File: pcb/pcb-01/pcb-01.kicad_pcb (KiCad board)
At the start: 4 copper layers, 78 x 58 mm, 167 parts, among them J1 POWER, J2 MOTOR, J3 HALL, J4 TEMP, J5 I2C, J6 USB-C, J7 PROGRAM, J8 DNP 2x5 1.27mm, Q1 DMP6023LE-13, Q2 2N7002K, Q3 2N7002, SW1 SW_Push, SW2 SW_Push, SW3 SW_Push, U1 MCF8316DVRGFR, U10 SN74LVC1G17DCKR, U11 SN74LVC1G17DCKR, U12 TPD2EUSB30, U2 ESP32-C6-MINI-1, U3 TPSM365R6V3RDNR, U4 TPS7A1601DGN, U5 SN74LVC1G74DCTR, U6 SN74LVC1G74DCTR, U7 TPS3435CAKAGDD, U8 LM2907M-14, U9 TLV1701DBV

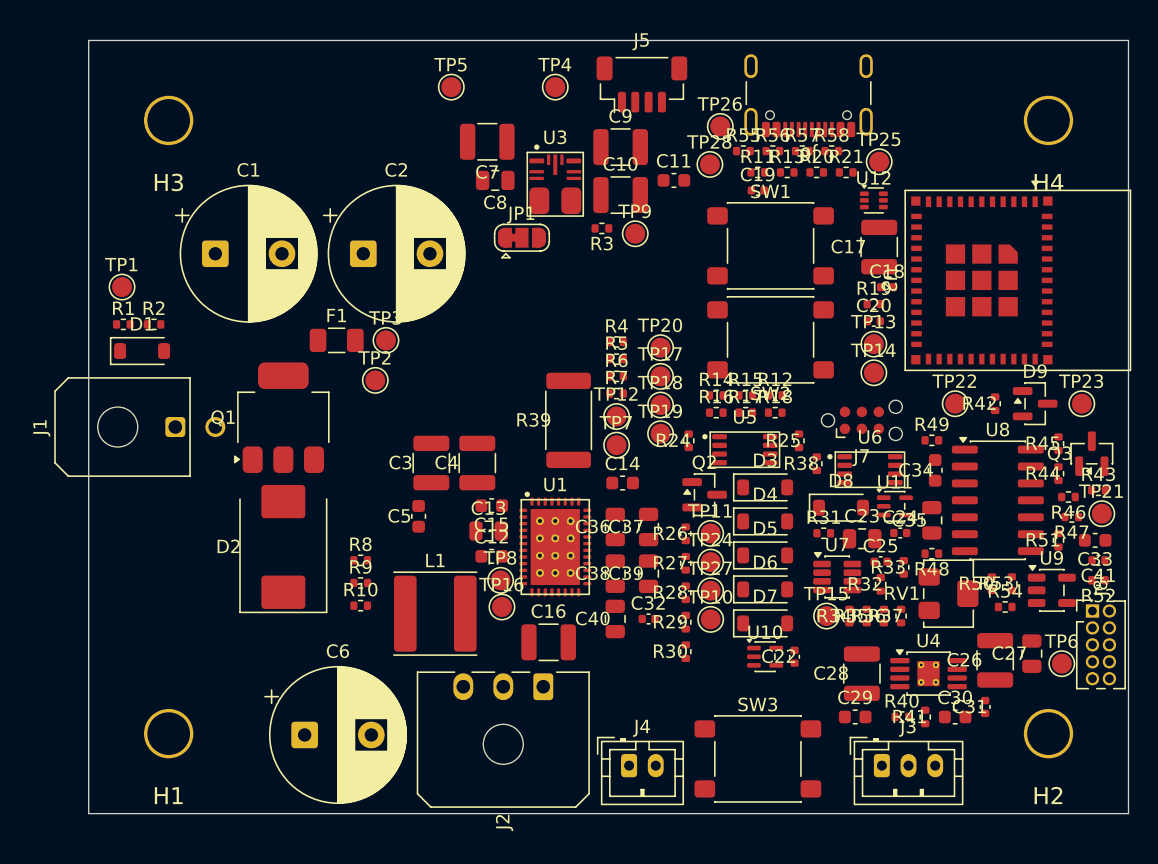
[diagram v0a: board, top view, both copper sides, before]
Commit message: pcb: aesthetic alignment pass on placement
Column/row alignment and grid snapping across all placement groups (62 parts
nudged): ESP resistor banks column-aligned, permission-cluster R/TP/D columns
on uniform pitch with aligned rows, mcf_east ladder+TP columns, lock_wd row
snapped, tach edge columns, LDO bottom row, DNP bank pitch equalized, R39
centered on U1's axis. Verified move-by-move against the exact courtyard
model (aes_check.py pattern: no gap regressions below 0.15mm except bodiless
test-point rings, documented). DRC: courtyards_overlap 16->17 (one TP ring
pair from uniform pitch), all other classes unchanged.
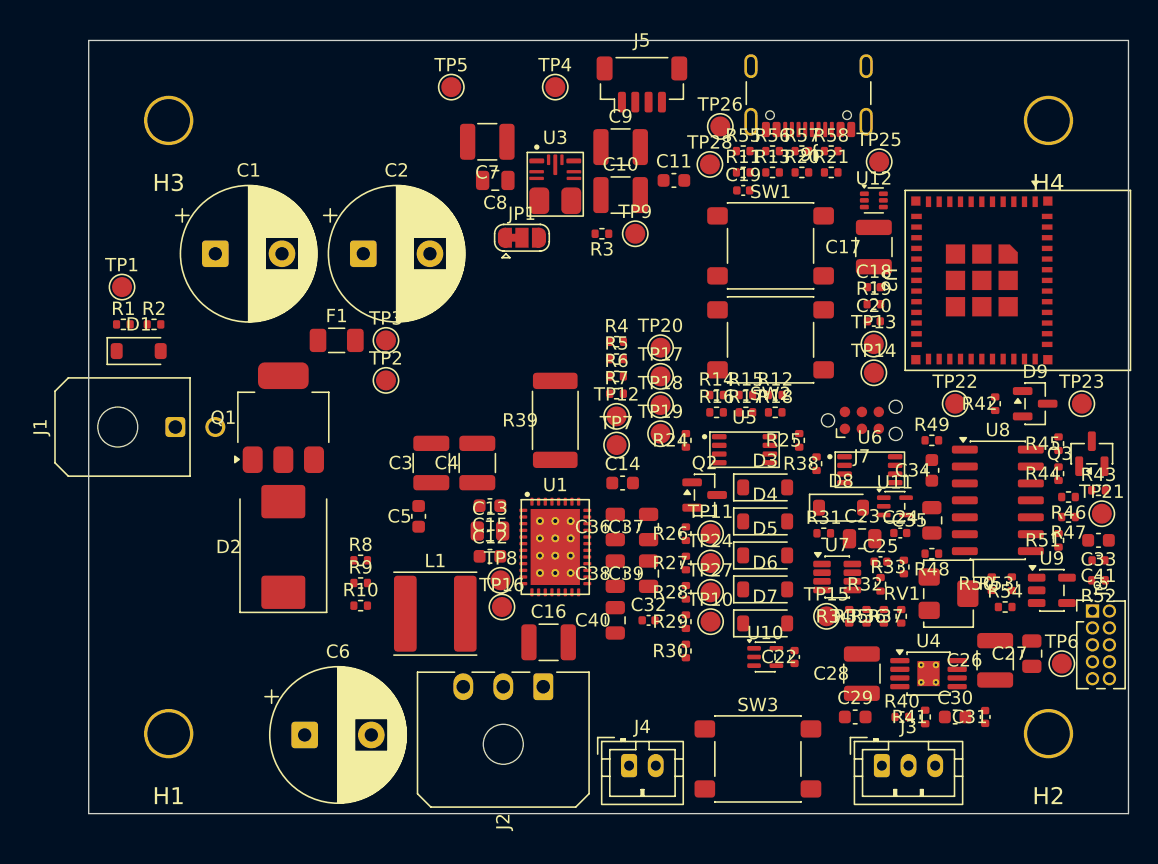
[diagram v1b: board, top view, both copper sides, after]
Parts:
- moved R21 1.12 mm to (105.7, 59.9)
- moved R20 1.11 mm to (103.5, 59.9)
- moved R13 1.10 mm to (101.3, 59.9)
- moved C19 1.09 mm to (99.1, 61.2)
- moved R11 1.09 mm to (99.1, 59.9)
- moved R39 1.00 mm to (85.0, 78.5)
- moved C18 0.99 mm to (108.9, 68.5)
- moved TP2 0.80 mm to (72.3, 75.5)
- moved C31 0.75 mm to (117.2, 100.8)
- moved R3 0.40 mm to (88.5, 64.5)
- moved C17 0.40 mm to (108.9, 65.5)
- moved D1 0.26 mm to (53.8, 73.3)
- moved C33 0.25 mm to (125.8, 87.5)
- moved C34 0.25 mm to (113.2, 82.2)
- moved R47 0.25 mm to (123.5, 85.8)
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
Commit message: pcb: board-side integration of review round 1
F8 sync applied (Michael), then placement of the changed parts: NT1 net-tie
at the PGND/AGND pour boundary north of C3/C4 (77, 77.95); J5 side-entry
SM04B re-seated at the top-left edge (71.8, 54) rot 180, cable exit north
over the edge, pads 0.6mm inside the copper-clearance line; C32 moved from
the DNP bank to the LM2907 input at (115.5, 79.16) next to R45/U8 pin 1
(TP22 nudged 0.1mm north for clearance); U12 kept in place on the smaller
DRT-3 footprint.

DRC improved: clearance 14 -> 10 (the U12 SOT-563 phantom fine-pitch pairs
are gone), silk_edge 6 -> 5, no new violations in any class.
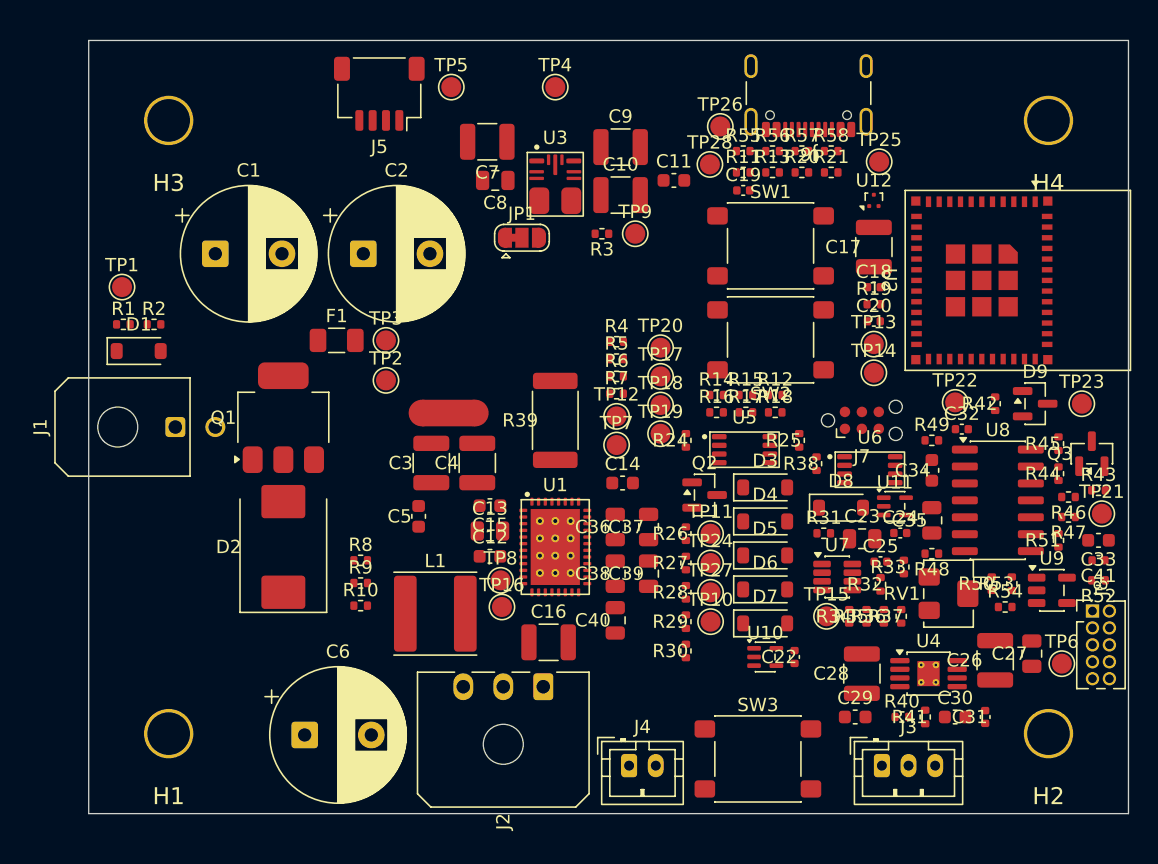
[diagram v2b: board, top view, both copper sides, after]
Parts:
- added NT1: PGND-AGND tie, NetTie:NetTie-2_SMD_Pad2.0mm, F.Cu at (77.0, 78.0)
- C17: value 22uF -> 22uF 25V X7R
- C36: value 470nF -> 470nF DNP
- C37: value 1uF -> 1uF DNP
- C38: value 3.3uF -> 3.3uF DNP
- C39: value 4.7uF -> 4.7uF DNP
- C40: value 6.8uF -> 6.8uF DNP
- J5: footprint Connector_JST:JST_SH_BM04B-SRSS-TB_1x04-1MP_P1.00mm_Vertical -> Connector_JST:JST_SH_SM04B-SRSS-TB_1x04-1MP_P1.00mm_Horizontal
- R43: value 100k -> 10k
- U12: footprint Package_TO_SOT_SMD:SOT-563 -> Package_TO_SOT_SMD:Texas_DRT-3
- moved C32 27.5 mm to (115.5, 79.2)
- moved J5 19.7 mm to (71.8, 54.0), turned to 180 degrees
- moved TP22 0.10 mm to (115.0, 77.2)
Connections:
- R3 pad 1: 3V3 -> /SCH-02 3V3 Rail/U3_VCC
- R43 pad 2: AGND -> 3V3

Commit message: pcb: place C42/C43 + proximity shuffle (C5 to U1 VM corner, C11/C34 tightened, TP8/TP16 column)
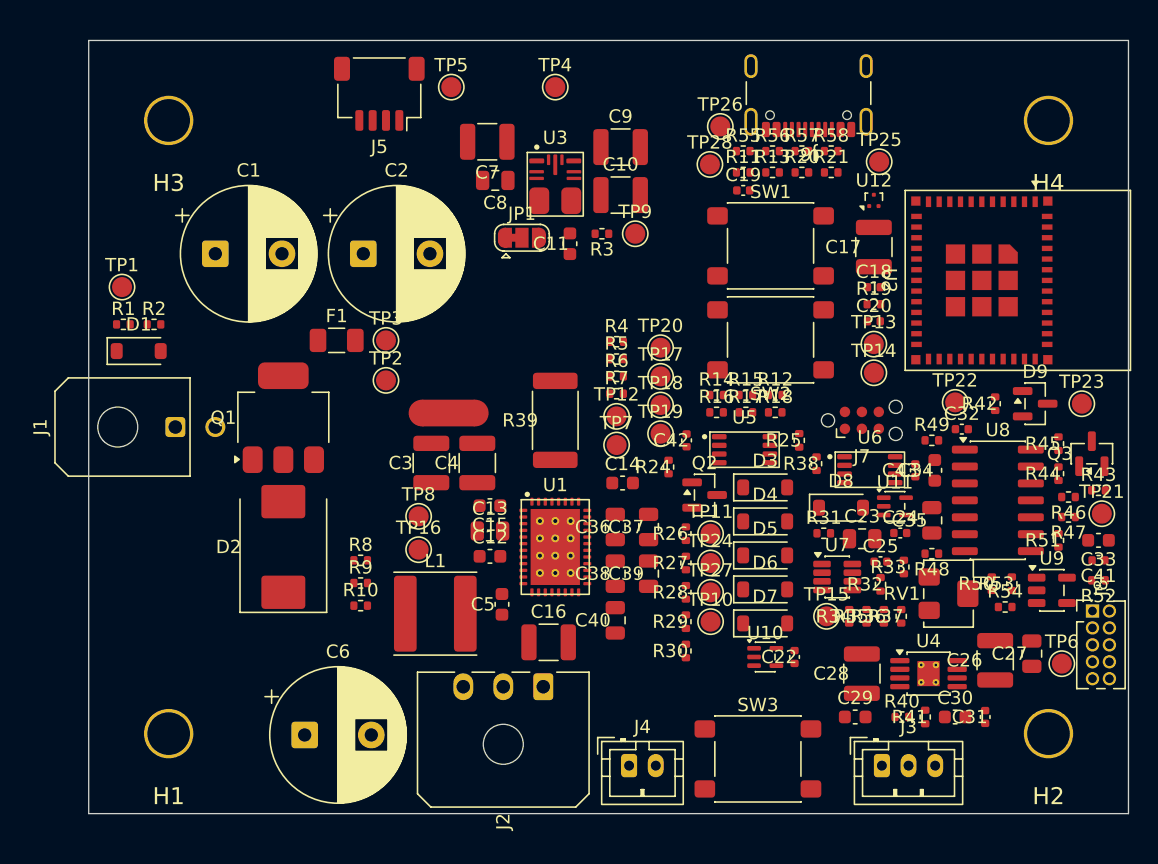
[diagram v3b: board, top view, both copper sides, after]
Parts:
- added C42: 100nF, Capacitor_SMD:C_0402_1005Metric, F.Cu at (94.8, 80.0)
- added C43: 100nF, Capacitor_SMD:C_0402_1005Metric, F.Cu at (112.0, 82.2)
- moved C11 9.13 mm to (86.1, 65.2), turned to 90 degrees
- moved C5 9.09 mm to (81.0, 92.3)
- moved TP8 7.80 mm to (74.8, 85.7)
- moved TP16 7.59 mm to (74.8, 88.2)
- moved R24 2.39 mm to (93.5, 82.0)
- moved C34 0.22 mm to (113.5, 82.2)

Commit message: pcb: layout locked — review loop converged at round 3 with GO verdict
Round 3 (delta-verify + fresh-eyes final gate): zero defects. The delta
lens confirmed R3's new PGOOD pull-up topology matches TI's own reference
schematic and improves power-up definedness, and caught C42 sitting on
U5's far side from VCC — fixed by swapping C42 with R25 (whose CLK-pulldown
net belongs on the west side anyway); C11 moved north of U3, 2.5mm from
the actual VCC pin. The fresh-eyes lens independently re-derived the full
ESP32 and latch pin maps clean, confirmed NT1 is the only ground bridge,
resolved the R22/R23/C21 ref gaps as renumbering debris, and found one
cross-subsystem config trap now in the register-image checklist:
EXT_WDT_CONFIG must be 500/1000ms (2Hz heartbeat can't satisfy the
100/200ms windows; 100ms is the chip's reset default).

waivers.md carries the lock declaration and the final 15-pair courtyard
residual list. Routing handoff: pours must meet ONLY at NT1; route USB as
J6 -> U12 -> module with no stub; silk ref cleanup after routing.
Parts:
- moved C11 8.75 mm to (85.2, 56.5)
- moved C42 8.45 mm to (103.3, 80.0)
- moved R25 8.45 mm to (94.8, 80.0)
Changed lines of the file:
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@@
 	(footprint "Capacitor_SMD:C_0402_1005Metric"
 		(layer "F.Cu")
-		(at 94.85 80 90)
+		(at 103.3 80 90)
 		(descr "Capacitor SMD 0402 (1005 Metric), square (rectangular) end terminal, IPC-7351 nominal, (Body size source: IPC-SM-782 page 76, https://www.pcb-3d.com/wordpress/wp-content/uploads/ipc-sm-782a_amendment_1_and_2.pdf)")
 		(tags "capacitor")
@@
 	(footprint "Resistor_SMD:R_0402_1005Metric"
 		(layer "F.Cu")
-		(at 103.3 80 90)
+		(at 94.85 80 90)
 		(descr "Resistor SMD 0402 (1005 Metric), square (rectangular) end terminal, IPC-7351 nominal, (Body size source: IPC-SM-782 page 72, https://www.pcb-3d.com/wordpress/wp-content/uploads/ipc-sm-782a_amendment_1_and_2.pdf)")
 		(tags "resistor")
@@
 	(footprint "Capacitor_SMD:C_0603_1608Metric"
 		(layer "F.Cu")
-		(at 86.1 65.25 90)
+		(at 85.2 56.55 90)
 		(descr "Capacitor SMD 0603 (1608 Metric), square (rectangular) end terminal, IPC-7351 nominal, (Body size source: IPC-SM-782 page 76, https://www.pcb-3d.com/wordpress/wp-content/uploads/ipc-sm-782a_amendment_1_and_2.pdf)")
 		(tags "capacitor")

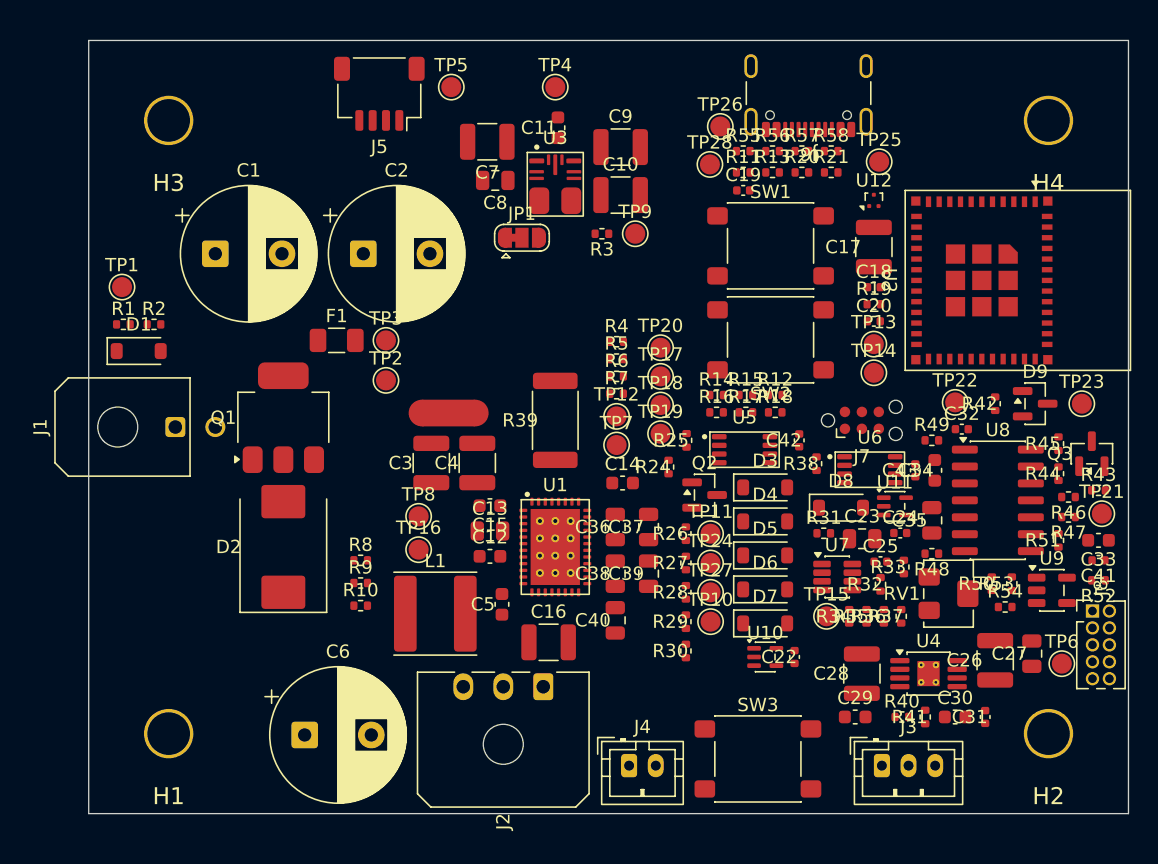
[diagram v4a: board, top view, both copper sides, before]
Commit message: pcb: route PCB-01 power, USB, ESP — mid-session checkpoint
L2 AGND plane + PGND island (NT1-only bridge), antenna keepout, phases
to J2 (U/W pins swapped for straight runs), MCF west cluster, input
stage, L3 split VM24/3V3 planes with via-storm distribution, 3V3
regulator, USB fan-out + FS diff pair, ESP power. Net classes actually
persisted to .kicad_pro (setup script had never run). C12/C15 rotated
180 as routing-driven placement fixes. Rationale in electrical.md
"Routing notes"; STATE.md reflects the checkpoint. Remaining: buck
loop, digital fan-out, tach analog, fills, silk sweep.
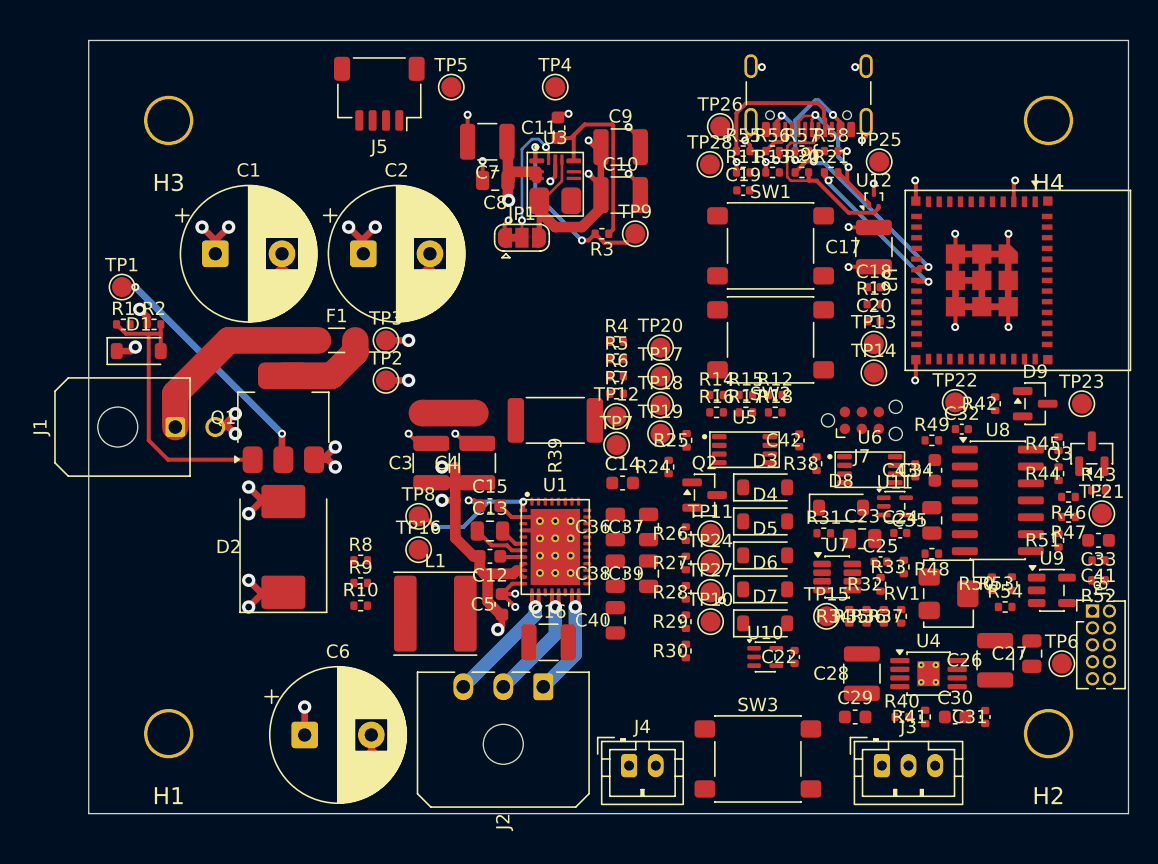
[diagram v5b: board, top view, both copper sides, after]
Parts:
- turned C12 to 180 degrees
- turned C15 to 0 degrees
- turned R39 to 180 degrees
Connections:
- J2 pad 1: PHASE_U -> PHASE_W
- J2 pad 3: PHASE_W -> PHASE_U
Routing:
- net AGND: track 0.00 -> 55.8 mm, vias 0 -> 21
- net VM24: track 0.00 -> 54.9 mm, vias 0 -> 16
- net PGND: track 0.00 -> 33.8 mm, vias 0 -> 16
- net 3V3: track 0.00 -> 26.0 mm, vias 0 -> 6
- net RAW24: track 0.00 -> 25.6 mm, vias 0 -> 2
- net /SCH-01 24V Input/PMOS_GATE: track 0.00 -> 22.0 mm
- net USB_DM: track 0.00 -> 15.4 mm
- net /SCH-07 Connectors/RAW24_IN: track 0.00 -> 14.9 mm
- net /SCH-02 3V3 Rail/U3_VCC: track 0.00 -> 14.8 mm
- net /SCH-04 ESP32-C6 Supervisor/ESP_USB_DM: track 0.00 -> 14.6 mm, vias 0 -> 2
- net PGOOD: track 0.00 -> 14.3 mm, vias 0 -> 2
- net USB_DP: track 0.00 -> 12.8 mm, vias 0 -> 2
- net /SCH-04 ESP32-C6 Supervisor/ESP_USB_DP: track 0.00 -> 12.4 mm, vias 0 -> 2
- net MCF_DVDD: track 0.00 -> 12.3 mm, vias 0 -> 3
- net /SCH-07 Connectors/CC1: track 0.00 -> 11.5 mm
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- added copper zone on In2.Cu, net 3V3
- added copper zone on In1.Cu, net AGND
- added copper zone on In1.Cu, net PGND
- added copper zone on In2.Cu, net VM24

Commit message: pcb: buck loop routed, NT1 ground tie made real — session wrap
C13/C15 column rearranged to open via space for the BUCK_SW/MCF_BUCK
B.Cu dives (board min via now 0.4/0.2). NT1's pad vias added — the
PGND/AGND tie was silently open (net-tie pads are F.Cu-only; no DRC
violation fires, only ratsnest). U1 pins 15/18 PGND escaped, R39 VM24
stitched. DRC at documented baseline, 276 ratsnest items remaining
(digital fan-out, tach analog, fills). Three new /pcb quirks: headless
DRC doesn't refill zones, net-tie via rule, zone-name dialog reuse.
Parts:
- moved C13 0.35 mm to (79.8, 86.8)
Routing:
- net /SCH-03 MCF Power Stage/MCF_BUCK: track 0.00 -> 17.2 mm, vias 0 -> 2
- net /SCH-03 MCF Power Stage/BUCK_SW: track 0.00 -> 11.6 mm, vias 0 -> 2
- net PGND: track 33.8 -> 36.5 mm, vias 16 -> 19
- net VM24: track 54.9 -> 57.5 mm, vias 16 -> 17
- net AGND: track 55.8 -> 57.5 mm, vias 21 -> 22
